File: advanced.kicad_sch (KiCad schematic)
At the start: 29 parts, among them U1 ATtiny24-20P, U2 ATtiny28L-4P, U3 ATtiny13A-P, U4 ATtiny25-20P, U5 ATtiny24-20P, U6 ATtiny85-20P

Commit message: slight progres
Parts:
- removed C7: C_Polarized, Capacitor_THT:CP_Axial_L10.0mm_D4.5mm_P15.00mm_Horizontal, symbol Device:C_Polarized
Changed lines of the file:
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@@
 (kicad_sch (version 20211123) (generator eeschema)
   (paper "A4")
-  (junction (at 229.87 77.47) (diameter 0) (color 0 0 0 0)
-  )
   (junction (at 96.52 123.19) (diameter 0) (color 0 0 0 0)
-  )
-  (junction (at 222.25 77.47) (diameter 0) (color 0 0 0 0)
   )
   (junction (at 73.66 172.72) (diameter 0) (color 0 0 0 0)
@@
   (symbol (lib_id "power:+5V") (at 88.9 66.04 0) (unit 1)
     (in_bom yes) (on_board yes) (fields_autoplaced)
-    (property "Reference" "#PWR?" (id 0) (at 88.9 69.85 0)
+    (property "Reference" "#PWR0103" (id 0) (at 88.9 69.85 0)
       (effects (font (size 1.27 1.27)) hide)
     )
@@
   (symbol (lib_id "power:Earth") (at 132.08 64.77 0) (unit 1)
     (in_bom yes) (on_board yes) (fields_autoplaced)
-    (property "Reference" "#PWR?" (id 0) (at 132.08 71.12 0)
+    (property "Reference" "#PWR0102" (id 0) (at 132.08 71.12 0)
       (effects (font (size 1.27 1.27)) hide)
     )
@@
   (symbol (lib_id "power:Earth") (at 88.9 111.76 0) (unit 1)
     (in_bom yes) (on_board yes) (fields_autoplaced)
-    (property "Reference" "#PWR?" (id 0) (at 88.9 118.11 0)
+    (property "Reference" "#PWR0104" (id 0) (at 88.9 118.11 0)
       (effects (font (size 1.27 1.27)) hide)
     )
@@
   (symbol (lib_id "power:+5V") (at 207.01 39.37 0) (unit 1)
     (in_bom yes) (on_board yes) (fields_autoplaced)
-    (property "Reference" "#PWR?" (id 0) (at 207.01 43.18 0)
+    (property "Reference" "#PWR0107" (id 0) (at 207.01 43.18 0)
       (effects (font (size 1.27 1.27)) hide)
     )
@@
   (symbol (lib_id "power:+5V") (at 234.95 107.95 0) (unit 1)
     (in_bom yes) (on_board yes) (fields_autoplaced)
-    (property "Reference" "#PWR?" (id 0) (at 234.95 111.76 0)
+    (property "Reference" "#PWR0110" (id 0) (at 234.95 111.76 0)
       (effects (font (size 1.27 1.27)) hide)
     )
@@
     (pin "1")
   )
-  (symbol (lib_id "Device:C_Polarized") (at 226.06 77.47 270) (unit 1)
-    (in_bom yes) (on_board yes) (fields_autoplaced)
-    (property "Reference" "C7" (id 0) (at 228.2191 81.28 0)
-      (effects (font (size 1.27 1.27)) (justify left))
-    )
-    (property "Value" "C_Polarized" (id 1) (at 225.6791 81.28 0)
-      (effects (font (size 1.27 1.27)) (justify left))
-    )
-    (property "Footprint" "Capacitor_THT:CP_Axial_L10.0mm_D4.5mm_P15.00mm_Horizontal" (id 2) (at 222.25 78.4352 0)
-      (effects (font (size 1.27 1.27)) hide)
-    )
-    (property "Datasheet" "~" (id 3) (at 226.06 77.47 0)
-      (effects (font (size 1.27 1.27)) hide)
-    )
-    (pin "1")
-    (pin "2")
-  )
   (symbol (lib_id "power:+5V") (at 170.18 111.76 0) (unit 1)
     (in_bom yes) (on_board yes) (fields_autoplaced)
-    (property "Reference" "#PWR?" (id 0) (at 170.18 115.57 0)
+    (property "Reference" "#PWR0109" (id 0) (at 170.18 115.57 0)
       (effects (font (size 1.27 1.27)) hide)
     )
@@
   (symbol (lib_id "power:+5V") (at 60.96 146.05 90) (unit 1)
     (in_bom yes) (on_board yes) (fields_autoplaced)
-    (property "Reference" "#PWR?" (id 0) (at 64.77 146.05 0)
+    (property "Reference" "#PWR0112" (id 0) (at 64.77 146.05 0)
       (effects (font (size 1.27 1.27)) hide)
     )
@@
   (symbol (lib_id "power:Earth") (at 132.08 146.05 90) (unit 1)
     (in_bom yes) (on_board yes) (fields_autoplaced)
-    (property "Reference" "#PWR?" (id 0) (at 138.43 146.05 0)
+    (property "Reference" "#PWR0111" (id 0) (at 138.43 146.05 0)
       (effects (font (size 1.27 1.27)) hide)
     )
@@
   (symbol (lib_id "power:Earth") (at 207.01 85.09 0) (unit 1)
     (in_bom yes) (on_board yes) (fields_autoplaced)
-    (property "Reference" "#PWR?" (id 0) (at 207.01 91.44 0)
+    (property "Reference" "#PWR0106" (id 0) (at 207.01 91.44 0)
       (effects (font (size 1.27 1.27)) hide)
     )
@@
   (symbol (lib_id "power:+5V") (at 132.08 34.29 0) (unit 1)
     (in_bom yes) (on_board yes) (fields_autoplaced)
-    (property "Reference" "#PWR?" (id 0) (at 132.08 38.1 0)
+    (property "Reference" "#PWR0105" (id 0) (at 132.08 38.1 0)
       (effects (font (size 1.27 1.27)) hide)
     )
@@
   (symbol (lib_id "power:Earth") (at 170.18 142.24 0) (unit 1)
     (in_bom yes) (on_board yes) (fields_autoplaced)
-    (property "Reference" "#PWR?" (id 0) (at 170.18 148.59 0)
+    (property "Reference" "#PWR0108" (id 0) (at 170.18 148.59 0)
       (effects (font (size 1.27 1.27)) hide)
     )
@@
       (reference "#PWR0101") (unit 1) (value "Earth") (footprint "")
     )
+    (path "/1d3090f6-2435-4bc3-9e98-932dfe0014d2"
+      (reference "#PWR0102") (unit 1) (value "Earth") (footprint "")
+    )
     (path "/0f8713c7-dddb-4560-b9b1-f772fa92c5ba"
-      (reference "#PWR?") (unit 1) (value "+5V") (footprint "")
-    )
-    (path "/1d3090f6-2435-4bc3-9e98-932dfe0014d2"
-      (reference "#PWR?") (unit 1) (value "Earth") (footprint "")
+      (reference "#PWR0103") (unit 1) (value "+5V") (footprint "")
     )
     (path "/2f461c25-1bbf-432b-b453-e2d655029513"
-      (reference "#PWR?") (unit 1) (value "Earth") (footprint "")
+      (reference "#PWR0104") (unit 1) (value "Earth") (footprint "")
+    )
+    (path "/f3defc7e-9af5-4f23-b019-b349f90ad509"
+      (reference "#PWR0105") (unit 1) (value "+5V") (footprint "")
+    )
+    (path "/a08da59d-26e0-4a55-8ba6-e2241011a1b6"
+      (reference "#PWR0106") (unit 1) (value "Earth") (footprint "")
     )
     (path "/30d5fabe-c42c-4296-90d2-7cbd65adfe12"
-      (reference "#PWR?") (unit 1) (value "+5V") (footprint "")
+      (reference "#PWR0107") (unit 1) (value "+5V") (footprint "")
+    )
+    (path "/f7695168-48ab-47b3-9182-facaccefa3fc"
+      (reference "#PWR0108") (unit 1) (value "Earth") (footprint "")
+    )
+    (path "/65638090-4be1-4b91-a36e-4da3471e35bc"
+      (reference "#PWR0109") (unit 1) (value "+5V") (footprint "")
     )
     (path "/3c84b99a-bf3e-47a4-9a99-9008a4467c45"
-      (reference "#PWR?") (unit 1) (value "+5V") (footprint "")
-    )
-    (path "/65638090-4be1-4b91-a36e-4da3471e35bc"
-      (reference "#PWR?") (unit 1) (value "+5V") (footprint "")
+      (reference "#PWR0110") (unit 1) (value "+5V") (footprint "")
+    )
+    (path "/823333a7-c053-419e-b611-938580f459b2"
+      (reference "#PWR0111") (unit 1) (value "Earth") (footprint "")
     )
     (path "/6e7b29b4-f70a-443e-92d4-ba9e25d738d0"
-      (reference "#PWR?") (unit 1) (value "+5V") (footprint "")
-    )
-    (path "/823333a7-c053-419e-b611-938580f459b2"
-      (reference "#PWR?") (unit 1) (value "Earth") (footprint "")
-    )
-    (path "/a08da59d-26e0-4a55-8ba6-e2241011a1b6"
-      (reference "#PWR?") (unit 1) (value "Earth") (footprint "")
-    )
-    (path "/f3defc7e-9af5-4f23-b019-b349f90ad509"
-      (reference "#PWR?") (unit 1) (value "+5V") (footprint "")
-    )
-    (path "/f7695168-48ab-47b3-9182-facaccefa3fc"
-      (reference "#PWR?") (unit 1) (value "Earth") (footprint "")
+      (reference "#PWR0112") (unit 1) (value "+5V") (footprint "")
     )
     (path "/f05521a7-4499-4f91-b508-afa00bf95d67"
@@
       (reference "C6") (unit 1) (value "C_Polarized") (footprint "Capacitor_THT:CP_Axial_L10.0mm_D4.5mm_P15.00mm_Horizontal")
     )
-    (path "/41f055e3-27f3-4cf9-99f0-07843f505d4b"
-      (reference "C7") (unit 1) (value "C_Polarized") (footprint "Capacitor_THT:CP_Axial_L10.0mm_D4.5mm_P15.00mm_Horizontal")
-    )
     (path "/c771b298-f03d-481f-9bb4-2d748e4fee4e"

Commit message: a
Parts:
- R1, R10, R11, R2, R3, R4, R5, R6, R7, R8, R9: footprint Resistor_THT:R_Axial_DIN0309_L9.0mm_D3.2mm_P25.40mm_Horizontal -> Resistor_THT:R_Axial_DIN0309_L9.0mm_D3.2mm_P15.24mm_Horizontal
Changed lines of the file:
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@@
     (property "Reference" "R8" (id 0) (at 125.73 124.46 90))
     (property "Value" "R" (id 1) (at 125.73 127 90))
-    (property "Footprint" "Resistor_THT:R_Axial_DIN0309_L9.0mm_D3.2mm_P25.40mm_Horizontal" (id 2) (at 125.73 132.588 90)
+    (property "Footprint" "Resistor_THT:R_Axial_DIN0309_L9.0mm_D3.2mm_P15.24mm_Horizontal" (id 2) (at 125.73 132.588 90)
       (effects (font (size 1.27 1.27)) hide)
     )
@@
       (effects (font (size 1.27 1.27)) (justify left))
     )
-    (property "Footprint" "Resistor_THT:R_Axial_DIN0309_L9.0mm_D3.2mm_P25.40mm_Horizontal" (id 2) (at 69.342 127 90)
+    (property "Footprint" "Resistor_THT:R_Axial_DIN0309_L9.0mm_D3.2mm_P15.24mm_Horizontal" (id 2) (at 69.342 127 90)
       (effects (font (size 1.27 1.27)) hide)
     )
@@
     (property "Reference" "R11" (id 0) (at 226.06 66.04 90))
     (property "Value" "R" (id 1) (at 226.06 68.58 90))
-    (property "Footprint" "Resistor_THT:R_Axial_DIN0309_L9.0mm_D3.2mm_P25.40mm_Horizontal" (id 2) (at 226.06 74.168 90)
+    (property "Footprint" "Resistor_THT:R_Axial_DIN0309_L9.0mm_D3.2mm_P15.24mm_Horizontal" (id 2) (at 226.06 74.168 90)
       (effects (font (size 1.27 1.27)) hide)
     )
@@
       (effects (font (size 1.27 1.27)) (justify left))
     )
-    (property "Footprint" "Resistor_THT:R_Axial_DIN0309_L9.0mm_D3.2mm_P25.40mm_Horizontal" (id 2) (at 82.042 127 90)
+    (property "Footprint" "Resistor_THT:R_Axial_DIN0309_L9.0mm_D3.2mm_P15.24mm_Horizontal" (id 2) (at 82.042 127 90)
       (effects (font (size 1.27 1.27)) hide)
     )
@@
       (effects (font (size 1.27 1.27)) (justify right))
     )
-    (property "Footprint" "Resistor_THT:R_Axial_DIN0309_L9.0mm_D3.2mm_P25.40mm_Horizontal" (id 2) (at 75.438 127 90)
+    (property "Footprint" "Resistor_THT:R_Axial_DIN0309_L9.0mm_D3.2mm_P15.24mm_Horizontal" (id 2) (at 75.438 127 90)
       (effects (font (size 1.27 1.27)) hide)
     )
@@
       (effects (font (size 1.27 1.27)) (justify left))
     )
-    (property "Footprint" "Resistor_THT:R_Axial_DIN0309_L9.0mm_D3.2mm_P25.40mm_Horizontal" (id 2) (at 107.95 93.218 90)
+    (property "Footprint" "Resistor_THT:R_Axial_DIN0309_L9.0mm_D3.2mm_P15.24mm_Horizontal" (id 2) (at 107.95 93.218 90)
       (effects (font (size 1.27 1.27)) hide)
     )
@@
     (property "Reference" "R6" (id 0) (at 109.22 92.71 90))
     (property "Value" "R" (id 1) (at 109.22 95.25 90))
-    (property "Footprint" "Resistor_THT:R_Axial_DIN0309_L9.0mm_D3.2mm_P25.40mm_Horizontal" (id 2) (at 109.22 100.838 90)
+    (property "Footprint" "Resistor_THT:R_Axial_DIN0309_L9.0mm_D3.2mm_P15.24mm_Horizontal" (id 2) (at 109.22 100.838 90)
       (effects (font (size 1.27 1.27)) hide)
     )
@@
       (effects (font (size 1.27 1.27)) (justify left))
     )
-    (property "Footprint" "Resistor_THT:R_Axial_DIN0309_L9.0mm_D3.2mm_P25.40mm_Horizontal" (id 2) (at 201.422 95.25 90)
+    (property "Footprint" "Resistor_THT:R_Axial_DIN0309_L9.0mm_D3.2mm_P15.24mm_Horizontal" (id 2) (at 201.422 95.25 90)
       (effects (font (size 1.27 1.27)) hide)
     )
@@
     (property "Reference" "R10" (id 0) (at 226.06 48.26 90))
     (property "Value" "R" (id 1) (at 226.06 50.8 90))
-    (property "Footprint" "Resistor_THT:R_Axial_DIN0309_L9.0mm_D3.2mm_P25.40mm_Horizontal" (id 2) (at 226.06 56.388 90)
+    (property "Footprint" "Resistor_THT:R_Axial_DIN0309_L9.0mm_D3.2mm_P15.24mm_Horizontal" (id 2) (at 226.06 56.388 90)
       (effects (font (size 1.27 1.27)) hide)
     )
@@
       (effects (font (size 1.27 1.27)) (justify left))
     )
-    (property "Footprint" "Resistor_THT:R_Axial_DIN0309_L9.0mm_D3.2mm_P25.40mm_Horizontal" (id 2) (at 76.962 165.1 90)
+    (property "Footprint" "Resistor_THT:R_Axial_DIN0309_L9.0mm_D3.2mm_P15.24mm_Horizontal" (id 2) (at 76.962 165.1 90)
       (effects (font (size 1.27 1.27)) hide)
     )
@@
     (property "Reference" "R7" (id 0) (at 115.57 85.09 90))
     (property "Value" "R" (id 1) (at 115.57 87.63 90))
-    (property "Footprint" "Resistor_THT:R_Axial_DIN0309_L9.0mm_D3.2mm_P25.40mm_Horizontal" (id 2) (at 115.57 93.218 90)
+    (property "Footprint" "Resistor_THT:R_Axial_DIN0309_L9.0mm_D3.2mm_P15.24mm_Horizontal" (id 2) (at 115.57 93.218 90)
       (effects (font (size 1.27 1.27)) hide)
     )
@@
     )
     (path "/25f2050d-fc88-48bc-8139-c68ef8e148c3"
-      (reference "R1") (unit 1) (value "R") (footprint "Resistor_THT:R_Axial_DIN0309_L9.0mm_D3.2mm_P25.40mm_Horizontal")
+      (reference "R1") (unit 1) (value "R") (footprint "Resistor_THT:R_Axial_DIN0309_L9.0mm_D3.2mm_P15.24mm_Horizontal")
     )
     (path "/a24956b0-ff86-4e8c-a4f1-6f0e903204c2"
-      (reference "R2") (unit 1) (value "R") (footprint "Resistor_THT:R_Axial_DIN0309_L9.0mm_D3.2mm_P25.40mm_Horizontal")
+      (reference "R2") (unit 1) (value "R") (footprint "Resistor_THT:R_Axial_DIN0309_L9.0mm_D3.2mm_P15.24mm_Horizontal")
     )
     (path "/eceb8dae-adf2-43c0-a9c5-dfd5fb785655"
-      (reference "R3") (unit 1) (value "R") (footprint "Resistor_THT:R_Axial_DIN0309_L9.0mm_D3.2mm_P25.40mm_Horizontal")
+      (reference "R3") (unit 1) (value "R") (footprint "Resistor_THT:R_Axial_DIN0309_L9.0mm_D3.2mm_P15.24mm_Horizontal")
     )
     (path "/90ec9a94-7420-48fe-ad7d-f6510b37df8b"
-      (reference "R4") (unit 1) (value "R") (footprint "Resistor_THT:R_Axial_DIN0309_L9.0mm_D3.2mm_P25.40mm_Horizontal")
+      (reference "R4") (unit 1) (value "R") (footprint "Resistor_THT:R_Axial_DIN0309_L9.0mm_D3.2mm_P15.24mm_Horizontal")
     )
     (path "/c1d0db41-bfdb-49e4-9ce3-41edf8979ea6"
-      (reference "R5") (unit 1) (value "R") (footprint "Resistor_THT:R_Axial_DIN0309_L9.0mm_D3.2mm_P25.40mm_Horizontal")
+      (reference "R5") (unit 1) (value "R") (footprint "Resistor_THT:R_Axial_DIN0309_L9.0mm_D3.2mm_P15.24mm_Horizontal")
     )
     (path "/cbf02271-dad1-4807-8e47-a1df4195221f"
-      (reference "R6") (unit 1) (value "R") (footprint "Resistor_THT:R_Axial_DIN0309_L9.0mm_D3.2mm_P25.40mm_Horizontal")
+      (reference "R6") (unit 1) (value "R") (footprint "Resistor_THT:R_Axial_DIN0309_L9.0mm_D3.2mm_P15.24mm_Horizontal")
     )
     (path "/f7bc00be-8280-4870-9a4d-7daa219d6a0f"
-      (reference "R7") (unit 1) (value "R") (footprint "Resistor_THT:R_Axial_DIN0309_L9.0mm_D3.2mm_P25.40mm_Horizontal")
+      (reference "R7") (unit 1) (value "R") (footprint "Resistor_THT:R_Axial_DIN0309_L9.0mm_D3.2mm_P15.24mm_Horizontal")
     )
     (path "/07736815-8c95-4fc2-ac10-3a62c0ac01d4"
-      (reference "R8") (unit 1) (value "R") (footprint "Resistor_THT:R_Axial_DIN0309_L9.0mm_D3.2mm_P25.40mm_Horizontal")
+      (reference "R8") (unit 1) (value "R") (footprint "Resistor_THT:R_Axial_DIN0309_L9.0mm_D3.2mm_P15.24mm_Horizontal")
     )
     (path "/d1b534f4-df0c-4731-8cc5-d2c195e8d0a8"
-      (reference "R9") (unit 1) (value "R") (footprint "Resistor_THT:R_Axial_DIN0309_L9.0mm_D3.2mm_P25.40mm_Horizontal")
+      (reference "R9") (unit 1) (value "R") (footprint "Resistor_THT:R_Axial_DIN0309_L9.0mm_D3.2mm_P15.24mm_Horizontal")
     )
     (path "/decfc5a3-4de4-447f-8519-61530d4a469c"
-      (reference "R10") (unit 1) (value "R") (footprint "Resistor_THT:R_Axial_DIN0309_L9.0mm_D3.2mm_P25.40mm_Horizontal")
+      (reference "R10") (unit 1) (value "R") (footprint "Resistor_THT:R_Axial_DIN0309_L9.0mm_D3.2mm_P15.24mm_Horizontal")
     )
     (path "/2c6f9eb8-5697-4256-af58-5bda58a787a6"
-      (reference "R11") (unit 1) (value "R") (footprint "Resistor_THT:R_Axial_DIN0309_L9.0mm_D3.2mm_P25.40mm_Horizontal")
+      (reference "R11") (unit 1) (value "R") (footprint "Resistor_THT:R_Axial_DIN0309_L9.0mm_D3.2mm_P15.24mm_Horizontal")
     )
     (path "/7d28f90d-c894-47ad-bc50-36846cfcc140"

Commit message: pathing done
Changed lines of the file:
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@@
   )
   (symbol (lib_id "MCU_Microchip_ATtiny:ATtiny28L-4P") (at 96.52 146.05 90) (unit 1)
-    (in_bom yes) (on_board yes) (fields_autoplaced)
+    (in_bom yes) (on_board yes)
     (property "Reference" "U2" (id 0) (at 137.16 142.4686 90))
-    (property "Value" "ATtiny28L-4P" (id 1) (at 137.16 145.0086 90))
+    (property "Value" "ATtiny28L-4P" (id 1) (at 135.89 140.97 90))
     (property "Footprint" "Package_DIP:DIP-28_W7.62mm" (id 2) (at 96.52 146.05 0)
       (effects (font (size 1.27 1.27) italic) hide)

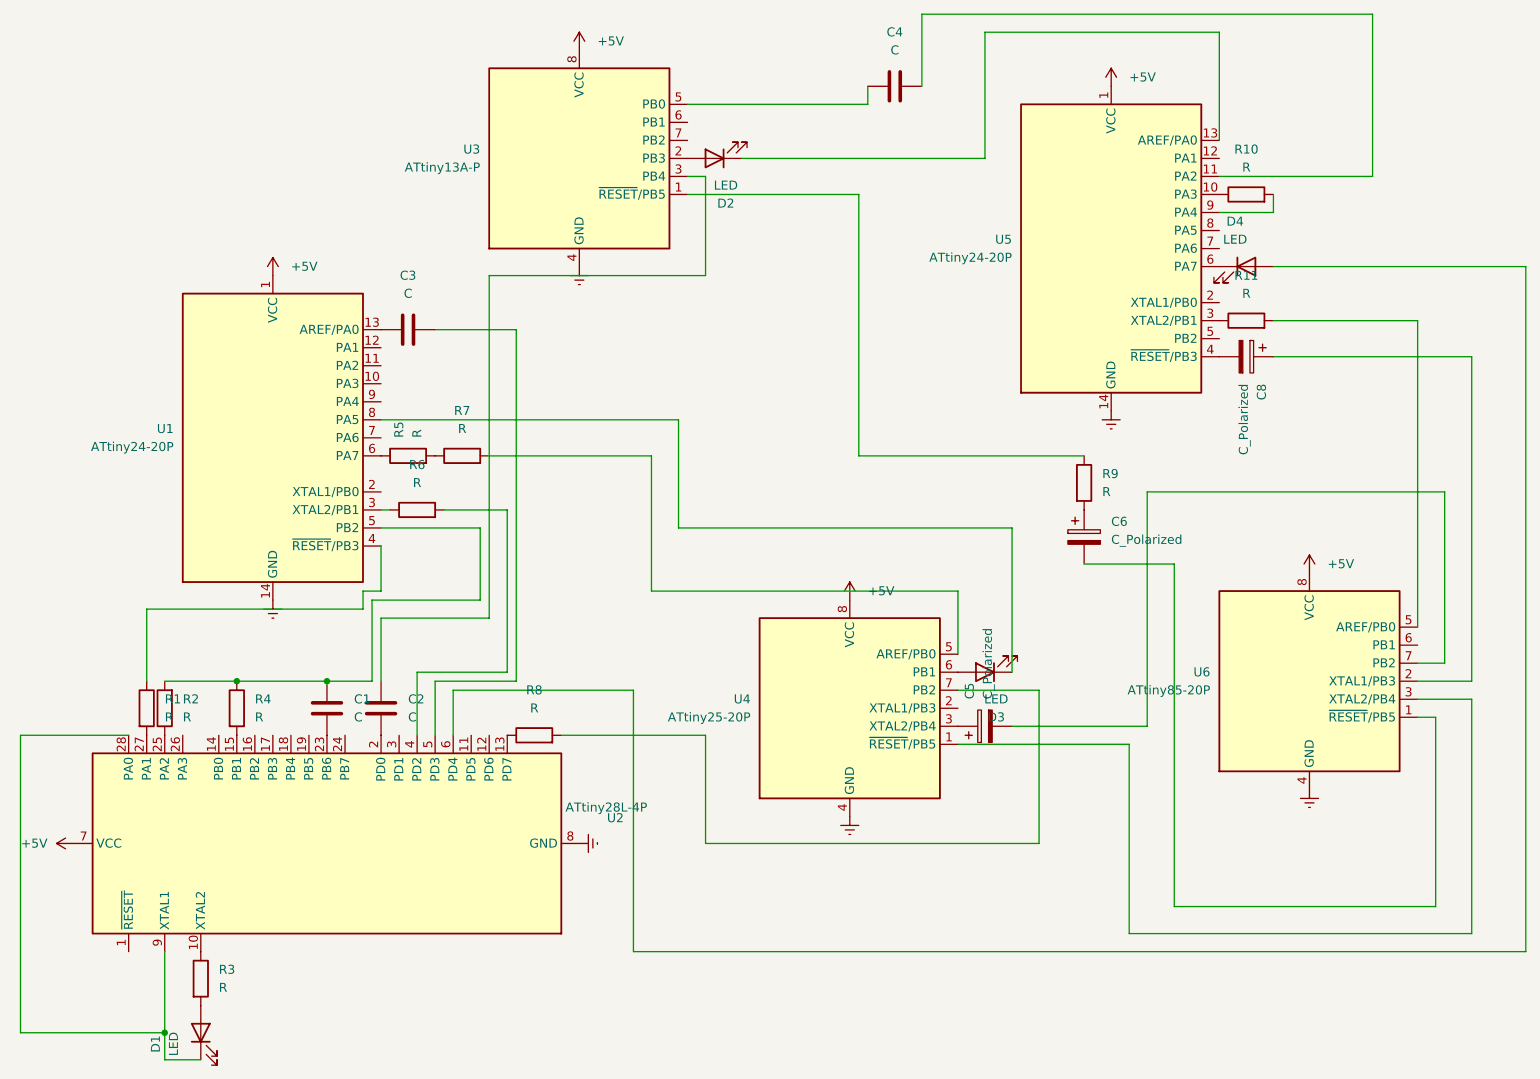
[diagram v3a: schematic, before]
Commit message: single ground, part list propably doneish
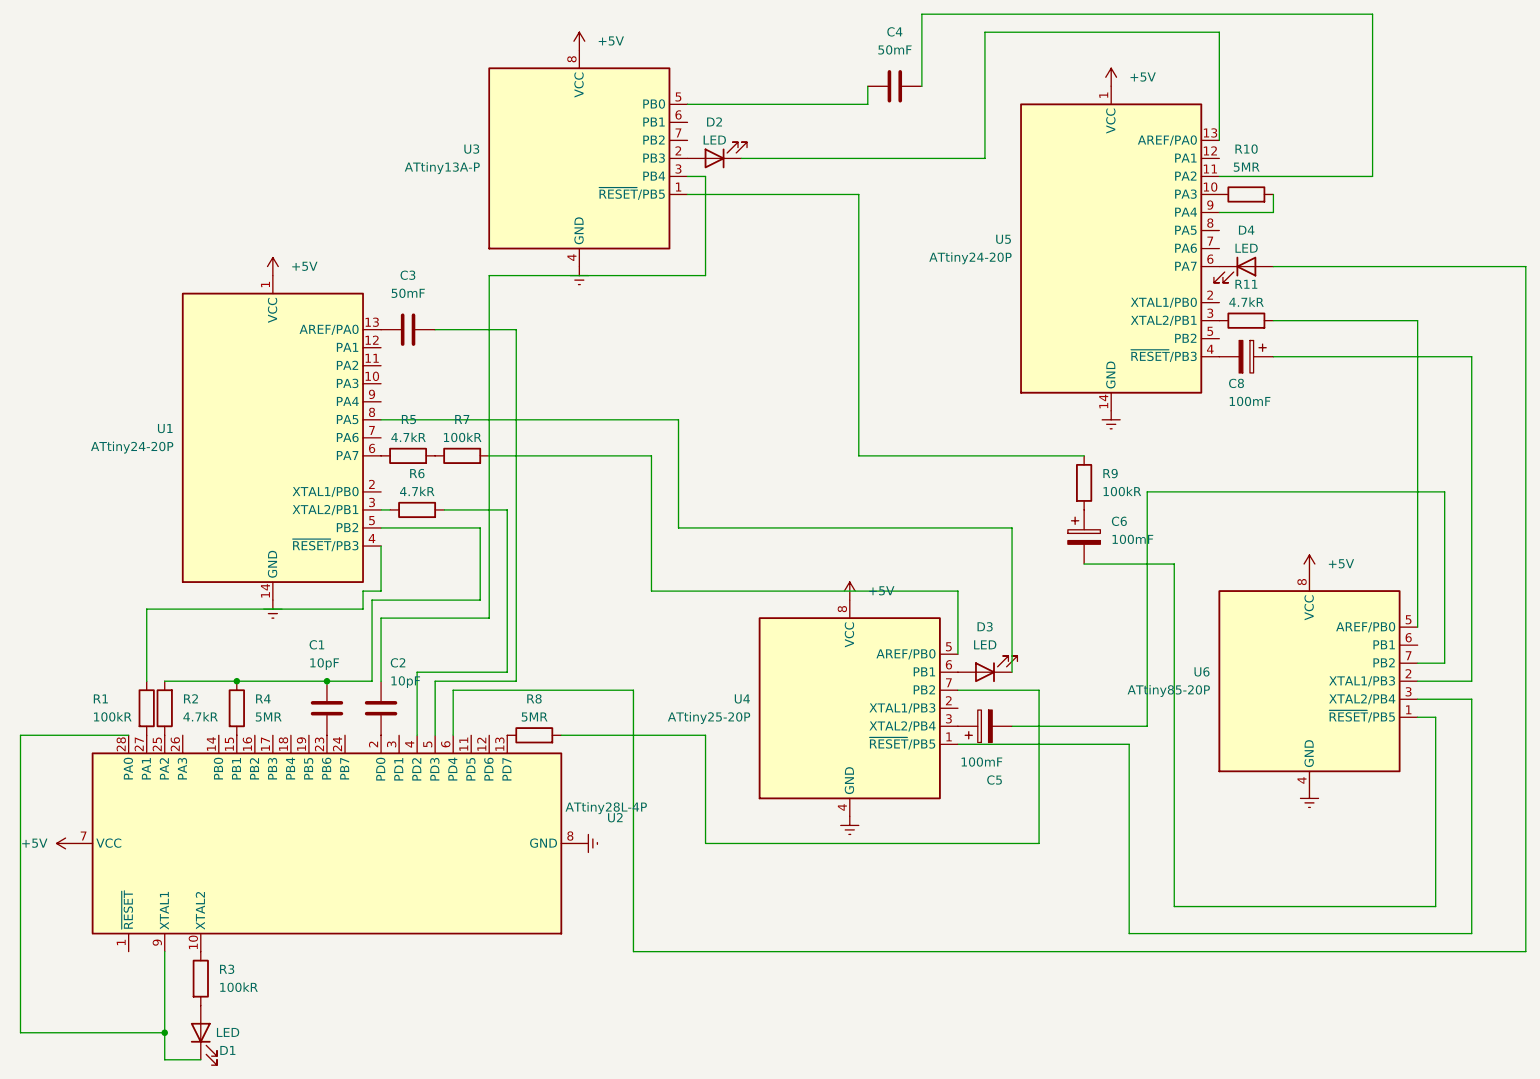
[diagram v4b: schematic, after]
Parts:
- C1, C2: value C -> 10pF
- C3, C4: value C -> 50mF
- C5, C6, C8: value C_Polarized -> 100mF
- R1, R3, R7, R9: value R -> 100kR
- R10, R4, R8: value R -> 5MR
- R11, R2, R5, R6: value R -> 4.7kR
